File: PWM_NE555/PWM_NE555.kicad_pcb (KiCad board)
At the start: 2 copper layers, 12 parts, among them J1 CONN_01X02, J2 CONN_01X02, J3 CONN_01X02, J4 CONN_01X02, U1 NE555

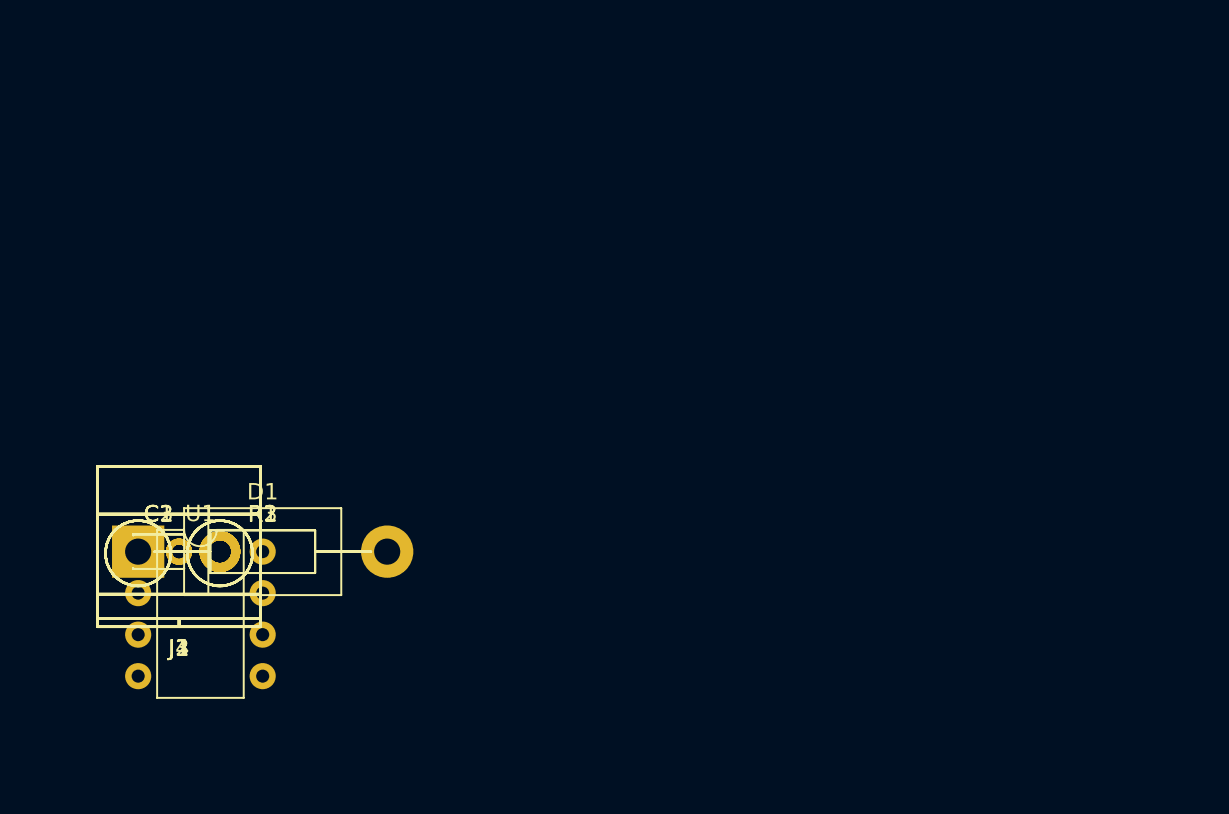
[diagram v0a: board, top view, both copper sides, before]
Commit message: Made PwM NE555 PCB Layout and Tracks
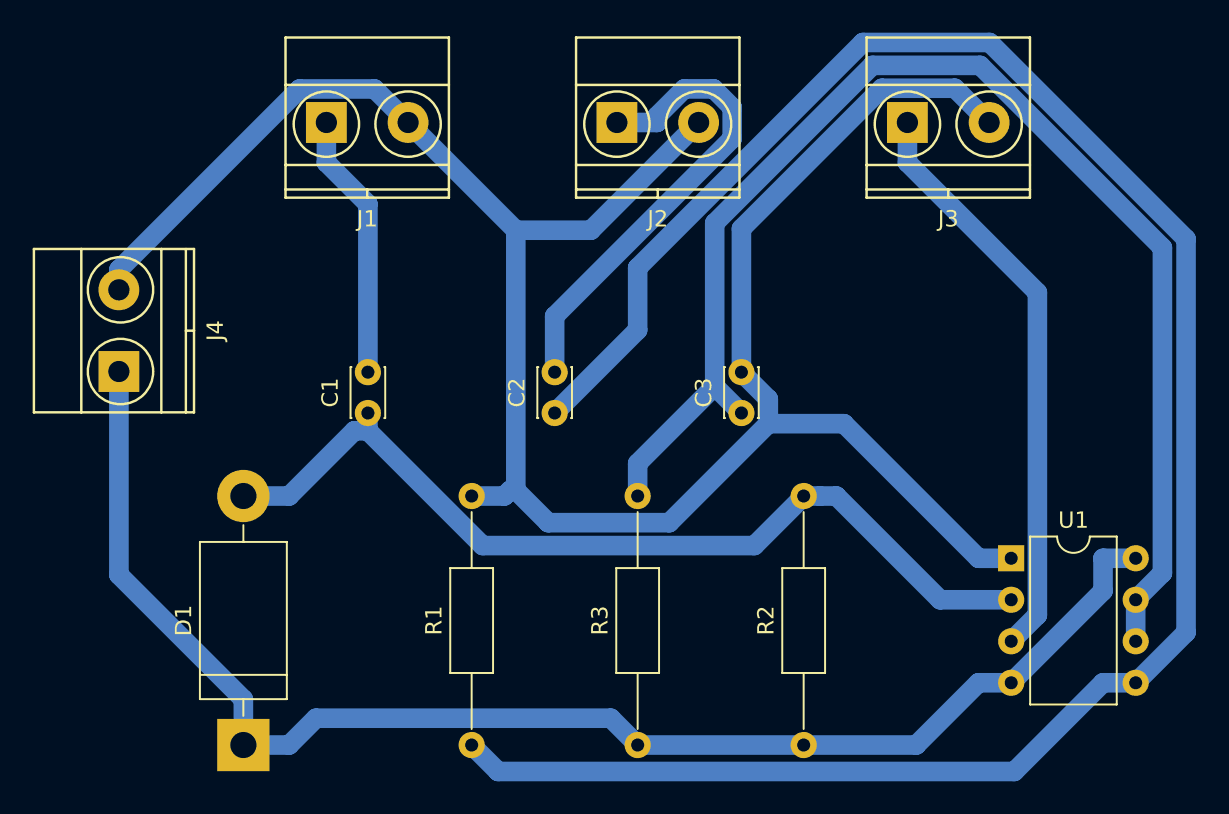
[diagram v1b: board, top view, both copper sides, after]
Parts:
- moved J3 53.9 mm to (195.6, 78.7)
- moved U1 53.4 mm to (201.9, 105.4)
- moved R2 42.4 mm to (189.2, 116.8), turned to 90 degrees
- moved J2 39.3 mm to (177.8, 78.7)
- moved C3 37.9 mm to (185.4, 96.5), turned to 90 degrees
- moved R3 32.8 mm to (179.1, 116.8), turned to 90 degrees
- moved J1 28.7 mm to (160.0, 78.7)
- moved C2 26.9 mm to (174.0, 96.5), turned to 90 degrees
- moved R1 23.6 mm to (168.9, 116.8), turned to 90 degrees
- moved C1 16.4 mm to (162.6, 96.5), turned to 90 degrees
- moved D1 13.5 mm to (154.9, 116.8), turned to 90 degrees
- moved J4 11.1 mm to (147.3, 94.0), turned to 90 degrees
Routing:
- net GND: track 0.00 -> 135.6 mm
- net Net-(C2-Pad1): track 0.00 -> 127.2 mm
- net /vcc: track 0.00 -> 87.9 mm
- net Net-(C3-Pad1): track 0.00 -> 81.8 mm
- net Net-(C1-Pad1): track 0.00 -> 56.5 mm
- net /op: track 0.00 -> 35.7 mm
- net Net-(C2-Pad2): track 0.00 -> 29.3 mm
- net Net-(C1-Pad2): track 0.00 -> 16.3 mm
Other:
- net class Default: clearance 0.2 -> 1
- rule trace_clearance: 0.2 -> 1
